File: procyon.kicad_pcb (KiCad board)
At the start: 4 copper layers, 42 x 49.6 mm, 34 parts, among them J1 Conn_01x07_Pin, Q1 AO3401A, U1 mXT336UD-MAU002

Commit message: Working changes
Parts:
- moved NT1 29.9 mm to (79.1, 97.6), turned to -135 degrees
- moved TP7 2.47 mm to (105.8, 80.3)
- moved TP1 1.26 mm to (82.9, 67.3)
- moved TP6 0.94 mm to (101.7, 84.7)
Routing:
- net /DBG_SS: track 32.2 -> 35.8 mm
- net /DBG_DATA: track 26.4 -> 29.4 mm
- net /DBG_CLK: track 27.0 -> 30.0 mm
- net /X5: track 59.1 -> 61.9 mm
- net /RESET: track 71.3 -> 73.8 mm
- net /SCL: track 47.7 -> 50.1 mm
- net /SDA: track 44.9 -> 47.2 mm
- net /CHANGE: track 54.5 -> 56.7 mm
- net /Y4: track 49.3 -> 51.4 mm
- net /Y5: track 51.9 -> 53.7 mm
- net /Y6: track 55.3 -> 57.1 mm
- net /Y10: track 69.2 -> 70.9 mm
- net /X6: track 62.4 -> 64.1 mm
- net /Y11: track 72.7 -> 74.2 mm
- net /POWER_CONTROL: track 30.8 -> 32.2 mm
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
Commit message: Flip the power control jumper.
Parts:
- turned JP2 to 0 degrees
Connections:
- JP2 pad 1: +3V3 IN -> GND
- JP2 pad 3: GND -> +3V3 IN
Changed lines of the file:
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@@
 	(footprint "Jumper:SolderJumper-3_P1.3mm_Bridged12_RoundedPad1.0x1.5mm_NumberLabels"
 		(layer "F.Cu")
-		(at 88.802099 72.54502 180)
+		(at 88.802099 72.54502)
 		(descr "SMD Solder 3-pad Jumper, 1x1.5mm rounded Pads, 0.3mm gap, pads 1-2 bridged with 1 copper strip, labeled with numbers")
 		(tags "net tie solder jumper bridged")
@@
 		)
 		(property "Footprint" "Jumper:SolderJumper-3_P1.3mm_Bridged12_RoundedPad1.0x1.5mm_NumberLabels"
-			(at 0 0 180)
+			(at 0 0 0)
 			(unlocked yes)
 			(layer "F.Fab")
@@
 		)
 		(property "Datasheet" ""
-			(at 0 0 180)
+			(at 0 0 0)
 			(unlocked yes)
 			(layer "F.Fab")
@@
 		)
 		(property "Description" "3-pole Solder Jumper, pins 1+2 closed/bridged"
-			(at 0 0 180)
+			(at 0 0 0)
 			(unlocked yes)
 			(layer "F.Fab")
@@
 		)
 		(fp_line
+			(start -2.05 0.3)
+			(end -2.05 -0.3)
+			(stroke
+				(width 0.12)
+				(type solid)
+			)
+			(layer "F.SilkS")
+		)
+		(fp_line
+			(start -1.4 -1)
+			(end 1.4 -1)
+			(stroke
+				(width 0.12)
+				(type solid)
+			)
+			(layer "F.SilkS")
+		)
+		(fp_line
+			(start 1.4 1)
+			(end -1.4 1)
+			(stroke
+				(width 0.12)
+				(type solid)
+			)
+			(layer "F.SilkS")
+		)
+		(fp_line
 			(start 2.05 -0.3)
 			(end 2.05 0.3)
@@
 			(layer "F.SilkS")
 		)
-		(fp_line
-			(start 1.4 1)
-			(end -1.4 1)
-			(stroke
-				(width 0.12)
-				(type solid)
-			)
-			(layer "F.SilkS")
-		)
-		(fp_line
-			(start -1.4 -1)
-			(end 1.4 -1)
-			(stroke
-				(width 0.12)
-				(type solid)
-			)
-			(layer "F.SilkS")
-		)
-		(fp_line
-			(start -2.05 0.3)
-			(end -2.05 -0.3)
+		(fp_arc
+			(start -2.05 -0.3)
+			(mid -1.844975 -0.794975)
+			(end -1.35 -1)
+			(stroke
+				(width 0.12)
+				(type solid)
+			)
+			(layer "F.SilkS")
+		)
+		(fp_arc
+			(start -1.35 1)
+			(mid -1.844975 0.794975)
+			(end -2.05 0.3)
+			(stroke
+				(width 0.12)
+				(type solid)
+			)
+			(layer "F.SilkS")
+		)
+		(fp_arc
+			(start 1.35 -1)
+			(mid 1.844975 -0.794975)
+			(end 2.05 -0.3)
 			(stroke
 				(width 0.12)
@@
 			(layer "F.SilkS")
 		)
-		(fp_arc
-			(start 1.35 -1)
-			(mid 1.844975 -0.794975)
-			(end 2.05 -0.3)
-			(stroke
-				(width 0.12)
-				(type solid)
-			)
-			(layer "F.SilkS")
-		)
-		(fp_arc
-			(start -1.35 1)
-			(mid -1.844975 0.794975)
-			(end -2.05 0.3)
-			(stroke
-				(width 0.12)
-				(type solid)
-			)
-			(layer "F.SilkS")
-		)
-		(fp_arc
-			(start -2.05 -0.3)
-			(mid -1.844975 -0.794975)
-			(end -1.35 -1)
-			(stroke
-				(width 0.12)
-				(type solid)
-			)
-			(layer "F.SilkS")
+		(fp_line
+			(start -2.3 -1.25)
+			(end -2.3 1.25)
+			(stroke
+				(width 0.05)
+				(type solid)
+			)
+			(layer "F.CrtYd")
+		)
+		(fp_line
+			(start -2.3 -1.25)
+			(end 2.3 -1.25)
+			(stroke
+				(width 0.05)
+				(type solid)
+			)
+			(layer "F.CrtYd")
+		)
+		(fp_line
+			(start 2.3 1.25)
+			(end -2.3 1.25)
+			(stroke
+				(width 0.05)
+				(type solid)
+			)
+			(layer "F.CrtYd")
 		)
 		(fp_line
@@
 			(layer "F.CrtYd")
 		)
-		(fp_line
-			(start 2.3 1.25)
-			(end -2.3 1.25)
-			(stroke
-				(width 0.05)
-				(type solid)
-			)
-			(layer "F.CrtYd")
-		)
-		(fp_line
-			(start -2.3 -1.25)
-			(end 2.3 -1.25)
-			(stroke
-				(width 0.05)
-				(type solid)
-			)
-			(layer "F.CrtYd")
-		)
-		(fp_line
-			(start -2.3 -1.25)
-			(end -2.3 1.25)
-			(stroke
-				(width 0.05)
-				(type solid)
-			)
-			(layer "F.CrtYd")
-		)
 		(fp_text user "OFF"
-			(at 3.75 -0.15 0)
+			(at 3.749999 -0.15 0)
 			(layer "F.SilkS")
 			(effects
@@
 		)
 		(fp_text user "ON"
-			(at -3.475 -0.2 0)
+			(at -3.475 -0.199999 0)
 			(layer "F.SilkS")
 			(effects
@@
 		)
 		(pad "1" smd custom
-			(at -1.3 0 180)
+			(at -1.3 0)
 			(size 1 0.5)
 			(layers "F.Cu" "F.Mask")
-			(net 3 "+3V3 IN")
+			(net 1 "GND")
 			(pinfunction "A")
 			(pintype "passive")
@@
 		)
 		(pad "2" smd rect
-			(at 0 0 180)
+			(at 0 0)
 			(size 1 1.5)
 			(layers "F.Cu" "F.Mask")
@@
 		)
 		(pad "3" smd custom
-			(at 1.3 0 180)
+			(at 1.3 0)
 			(size 1 0.5)
 			(layers "F.Cu" "F.Mask")
-			(net 1 "GND")
+			(net 3 "+3V3 IN")
 			(pinfunction "B")
 			(pintype "passive")

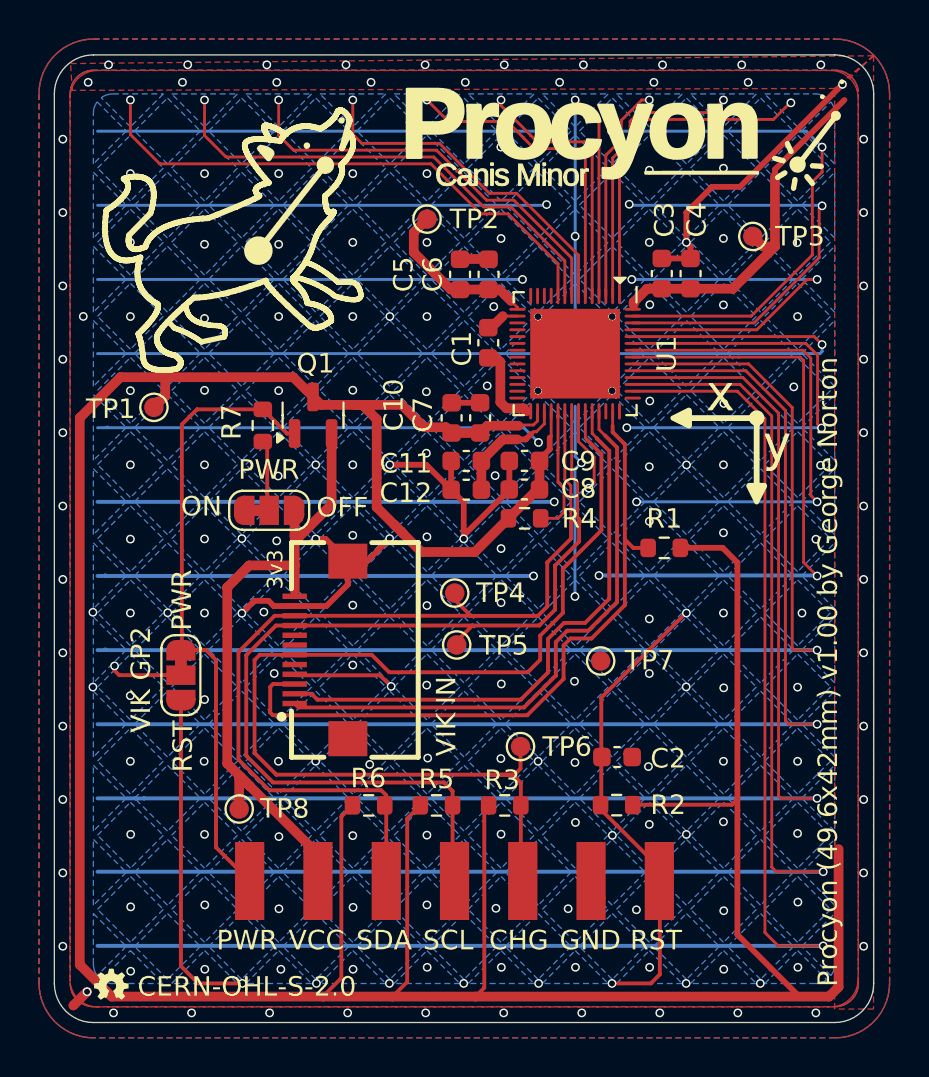
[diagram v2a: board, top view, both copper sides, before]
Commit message: Shuffle components to make space for more Y lines.
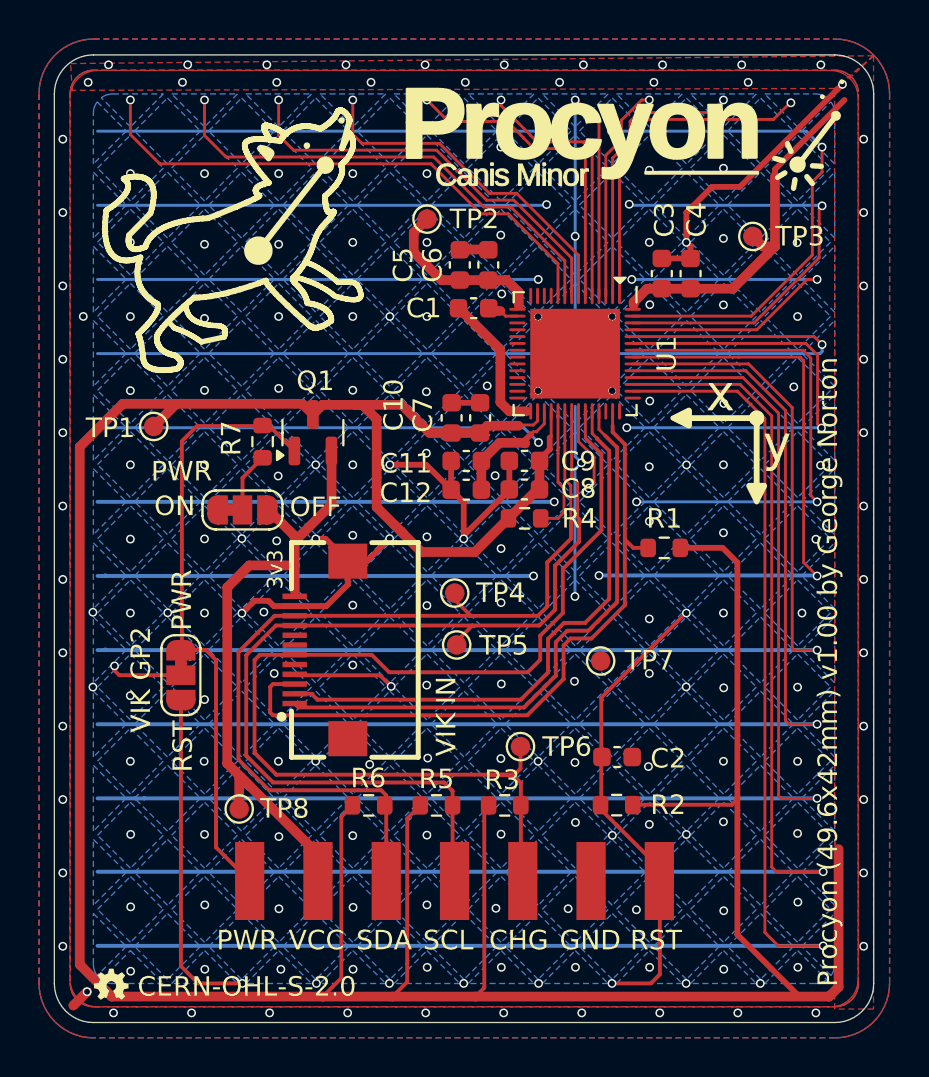
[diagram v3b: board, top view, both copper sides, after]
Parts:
- moved C1 1.92 mm to (99.3, 62.2), turned to 180 degrees
- moved JP2 1.37 mm to (87.4, 72.5)
- moved TP1 0.98 mm to (82.9, 68.2)
- moved Q1 0.90 mm to (91.0, 68.6)
- moved R7 0.83 mm to (88.5, 69.0)
- moved C6 0.48 mm to (100.0, 60.0)
- moved C5 0.48 mm to (98.6, 60.0)
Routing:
- net Net-(U1-EXCAP0): track 4.52 -> 7.47 mm
- net +3.3V: track 206.0 -> 204.3 mm
- net /POWER_CONTROL: track 32.2 -> 31.4 mm
- net Net-(JP2-C): track 3.66 -> 3.10 mm
- net /XVDD: track 8.57 -> 9.12 mm
